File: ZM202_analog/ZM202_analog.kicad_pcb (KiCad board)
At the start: 4 copper layers, 85 x 56 mm, 107 parts, among them J1 Conn_2x12_2.54_male, J2 Conn_Screw_1x4_male, T1 BC846BLT1G, T2 BC856B, T3 BC846BLT1G, T4 BC846BLT1G, U1 LM324, U10 TLC2272, U11 CD4052B, U14 CD4027, U15 LM393B, U16 LM358B, U18 BZX348, U3 TL431, U4 1N4148, U5 1N4148, U6 2N4416, U7 LM358B, U8 TLC2272

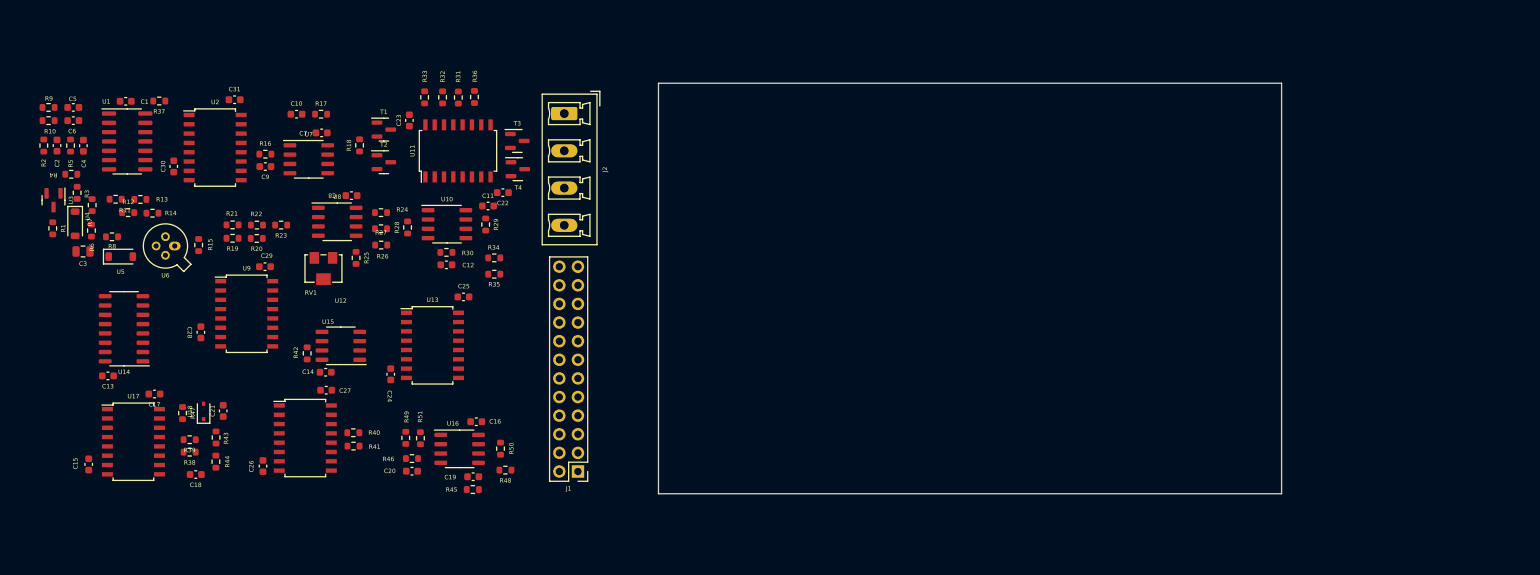
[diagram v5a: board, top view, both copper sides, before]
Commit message: 2-Layer design with 5V connections missing.
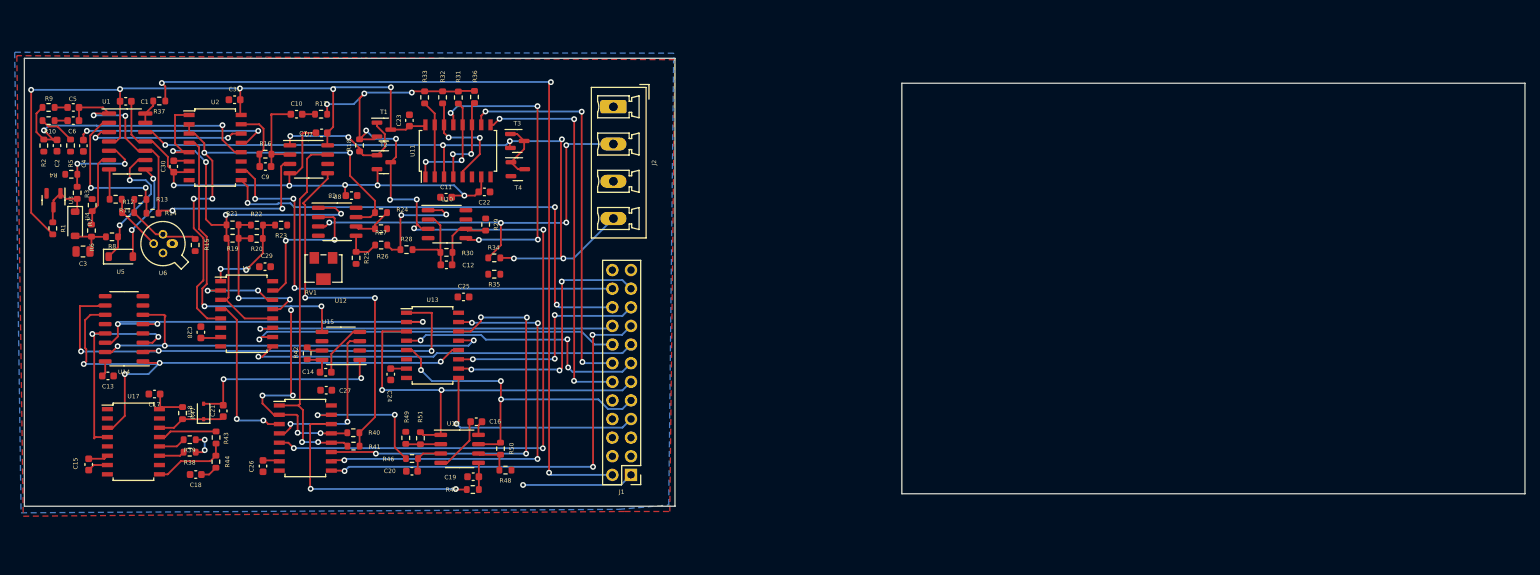
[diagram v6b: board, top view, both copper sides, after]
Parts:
- moved J1 7.25 mm to (105.2, 83.6)
- moved J2 6.76 mm to (102.8, 33.4)
- moved C11 5.85 mm to (80.0, 45.7)
- moved R28 3.03 mm to (74.5, 52.9), turned to 0 degrees
- moved C22 2.53 mm to (85.2, 45.0)
- moved R15 0.48 mm to (45.7, 52.2)
- moved U6 0.47 mm to (42.6, 52.0)
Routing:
- net /AnalogCore/V_sig: track 0.00 -> 139.5 mm, vias 0 -> 11
- net +5V: track 0.00 -> 129.8 mm, vias 0 -> 6
- net /AnalogCore/GUARD: track 0.00 -> 117.9 mm, vias 0 -> 3
- net -5V: track 0.00 -> 100.2 mm, vias 0 -> 5
- net /AnalogCore/DR+: track 0.00 -> 97.4 mm, vias 0 -> 6
- net /PLL/PHI0: track 0.00 -> 77.7 mm, vias 0 -> 4
- net /AnalogCore/VXX: track 0.00 -> 75.7 mm, vias 0 -> 7
- net /PLL/PHI180: track 0.00 -> 68.5 mm, vias 0 -> 3
- net /AnalogCore/C/L: track 0.00 -> 66.9 mm, vias 0 -> 3
- net /AnalogCore/VIX: track 0.00 -> 66.4 mm, vias 0 -> 4
- net /AnalogCore/VSRC: track 0.00 -> 65.9 mm, vias 0 -> 3
- net /AnalogCore/VVX: track 0.00 -> 65.8 mm, vias 0 -> 4
- net /PLL/PHI90: track 0.00 -> 60.3 mm, vias 0 -> 3
- net /PLL/PHSCAL: track 0.00 -> 59.7 mm, vias 0 -> 3
- net Net-(U12B-B): track 0.00 -> 57.7 mm, vias 0 -> 4
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- added copper zone on B.Cu, net GND
- added copper zone on F.Cu, net GND
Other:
- board size 85 x 56 mm -> 204.7 x 61.1 mm
- copper layers 4 -> 2
